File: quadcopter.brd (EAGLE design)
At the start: 228.6 x 228.6 mm, 62 parts, among them J1 AVR_SPI_PRG_6NS, U1 ATMEGA128RFA1, Y1 16MHz

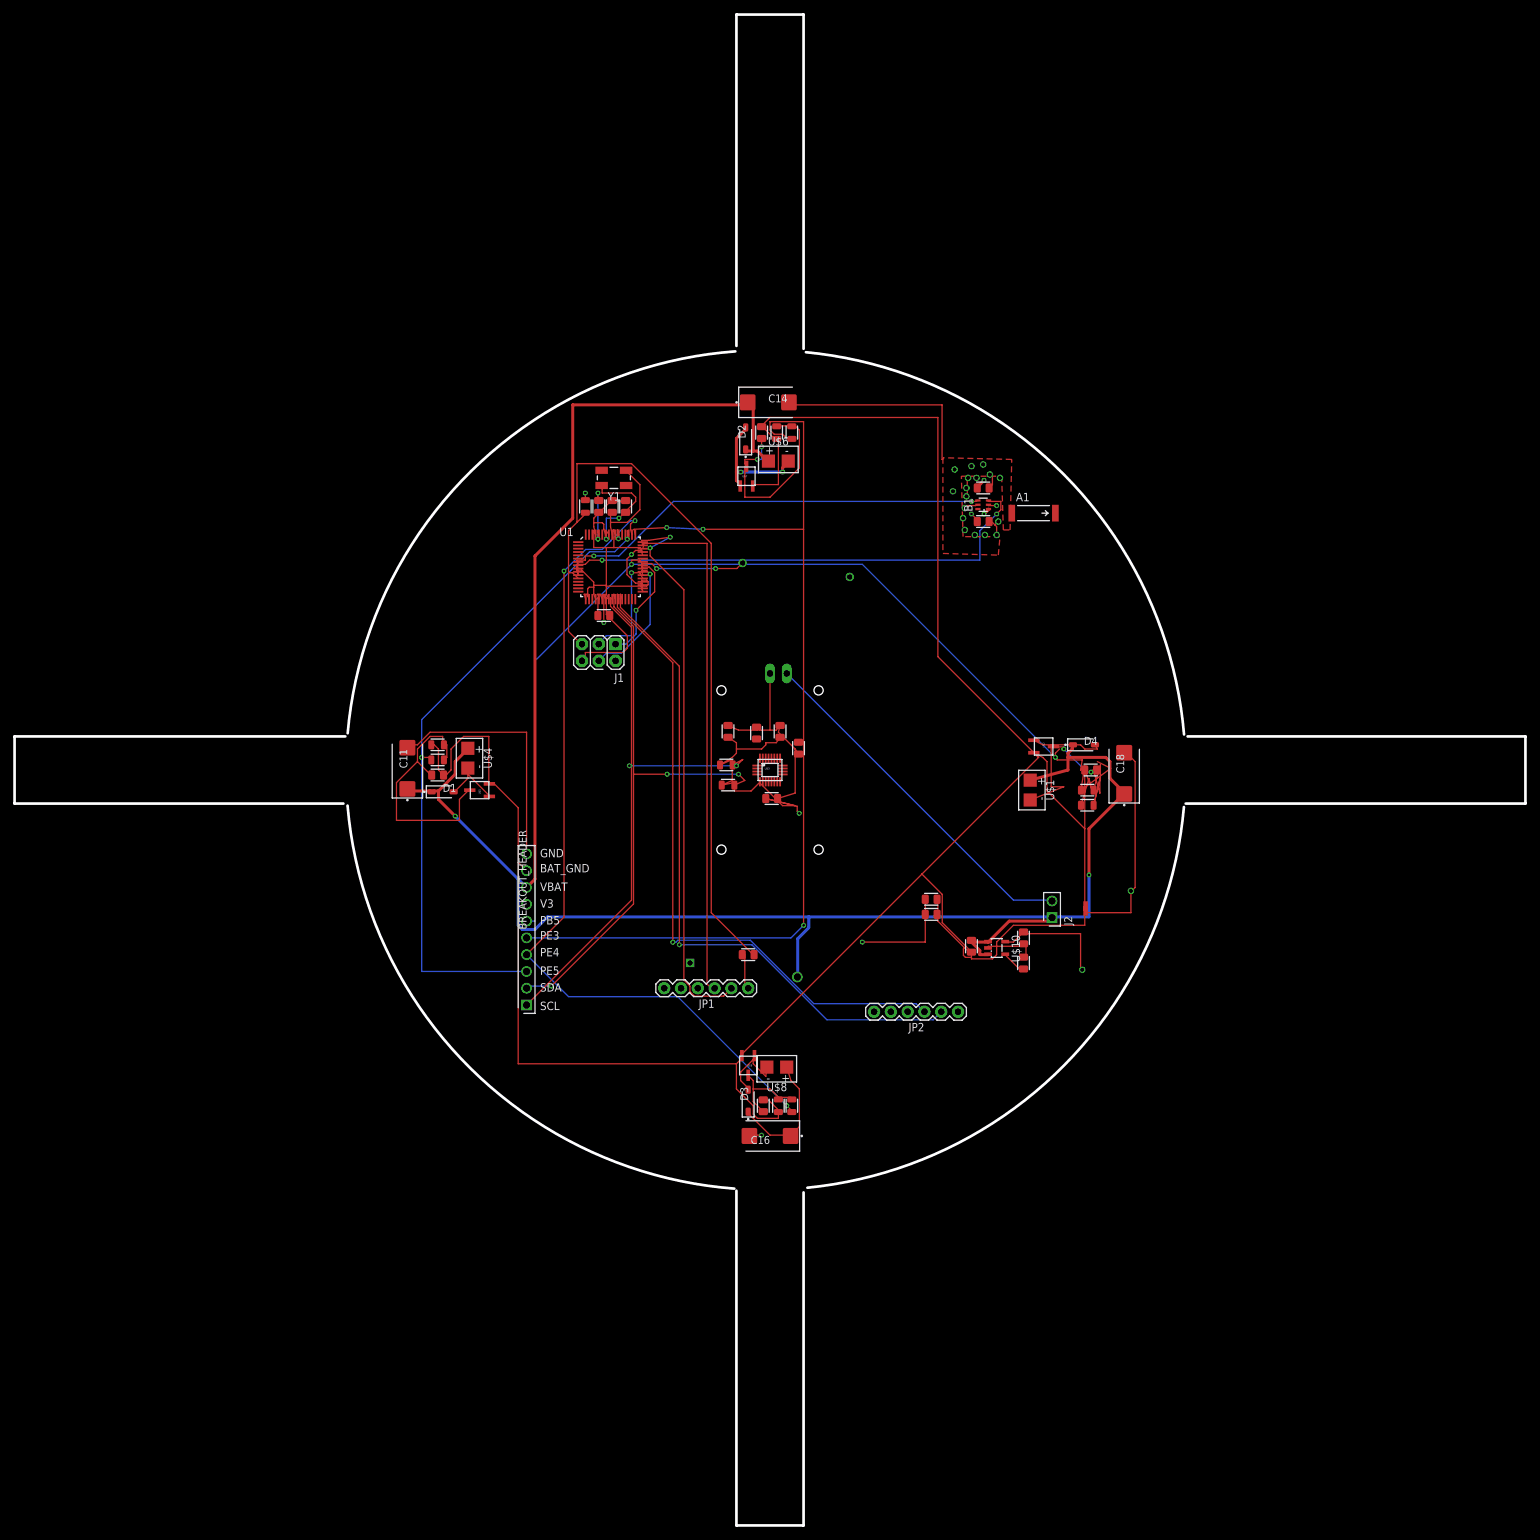
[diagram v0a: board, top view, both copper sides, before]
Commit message: Renamed schematics
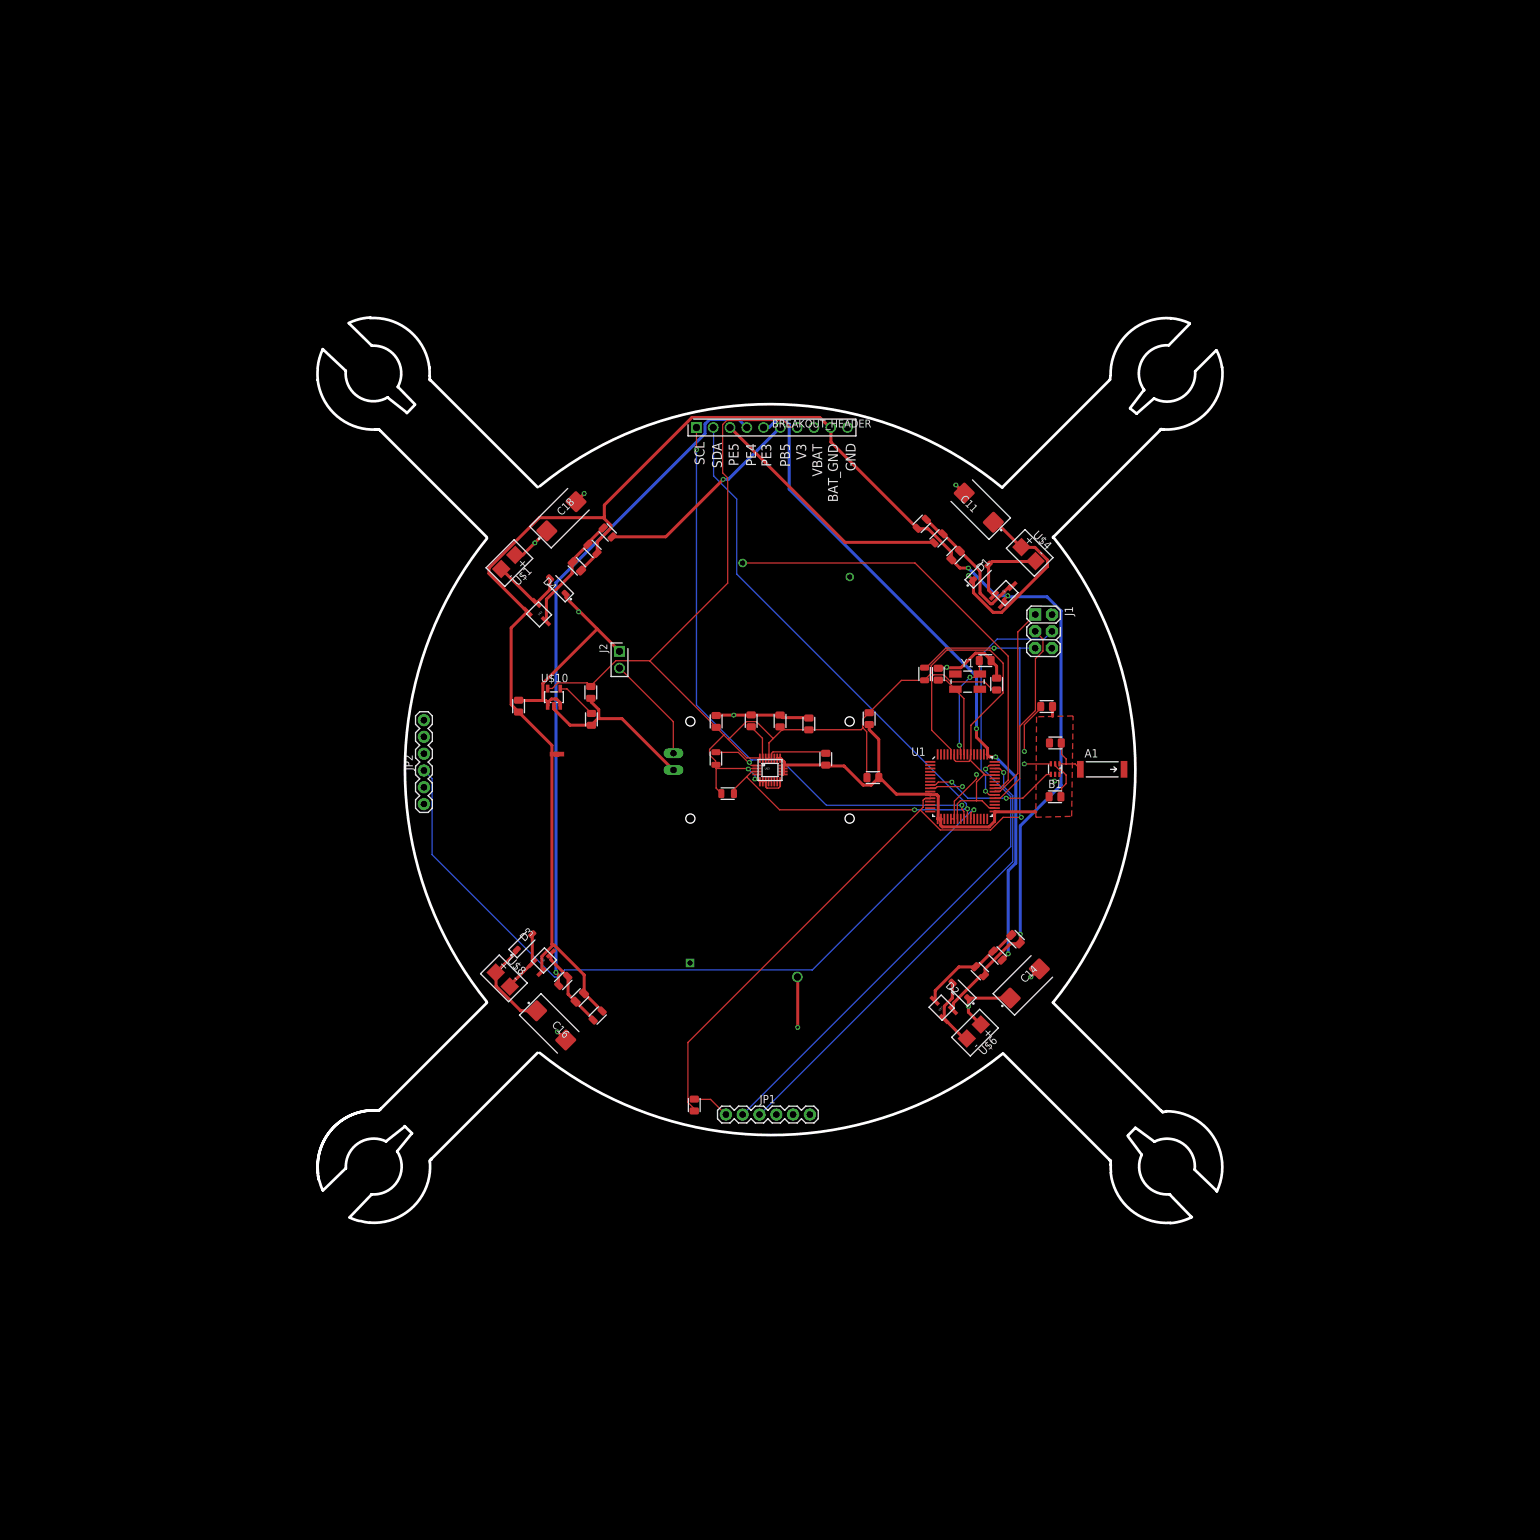
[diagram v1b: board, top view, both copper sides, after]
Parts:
- moved C14 96.1 mm to (38.5, -32.3), turned to 45 degrees
- moved C11 95.0 mm to (31.6, 39.7), turned to 135 degrees
- moved C18 93.6 mm to (-31.6, 38.4), turned to 45 degrees
- moved U$6 91.2 mm to (31.2, -39.2), turned to 225 degrees
- moved BREAKOUT_HEADER 91.1 mm to (-11.1, 51.8), turned to 0 degrees
- moved U$4 89.9 mm to (38.8, 33.0), turned to 315 degrees
- moved D2 89.6 mm to (28.8, -33.4), turned to 135 degrees
- moved D1 87.9 mm to (31.9, 29.9), turned to 45 degrees
- moved R8 87.1 mm to (31.8, -30.4), turned to 135 degrees
- moved JP2 86.7 mm to (-52.4, -5.15), turned to 90 degrees
- moved U$1 85.8 mm to (-39.2, 31.8), turned to 225 degrees
- moved C13 85.7 mm to (37.1, -25.6), turned to 315 degrees
- moved U$7 85.7 mm to (26.0, -36.0), turned to 45 degrees
- moved C7 85.1 mm to (28.1, 32.5), turned to 225 degrees
- moved R7 85.0 mm to (34.4, -28.1), turned to 135 degrees
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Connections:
- net GND: now also JP2.GND
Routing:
- net VBAT: track 313.5 -> 89.5 mm, vias 2 -> 5
- net GND: track 269.3 -> 121.5 mm, vias 19 -> 7
- net PB5: track 160.1 -> 32.3 mm, vias 2 -> 1
- net V3: track 97.3 -> 220.8 mm, vias 7 -> 2
- net TX1: track 102.3 -> 0.00 mm, vias 1 -> 0
- net BAT_GND: track 346.8 -> 272.5 mm, vias 0 -> 3
- net PE5: track 100.0 -> 38.1 mm, vias 2 -> 0
- net N$37: track 74.1 -> 19.8 mm
- net PE3: track 155.6 -> 101.3 mm
- net PB4: track 16.7 -> 67.3 mm, vias 2 -> 0
- net N$36: track 65.5 -> 20.9 mm
- net N$25: track 54.4 -> 16.3 mm
- net SDA: track 89.3 -> 115.9 mm, vias 3 -> 2
- net PE4: track 126.9 -> 101.6 mm, vias 3 -> 1
- net N$41: track 4.85 -> 25.1 mm, vias 0 -> 2
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- added copper zone on layer 15, net GND
- added copper zone on layer 15, net N$30
- added copper zone on layer 2, net N$30
- added copper zone on layer 2, net V3
- added copper zone on layer 2, net VBAT
- removed copper zone on layer 15, net N$3
- removed copper zone on layer 2, net N$3
- removed copper zone on layer 15, net V3
- removed copper zone on layer 15, net VBAT
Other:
- board size 228.6 x 228.6 mm -> 136.9 x 137 mm

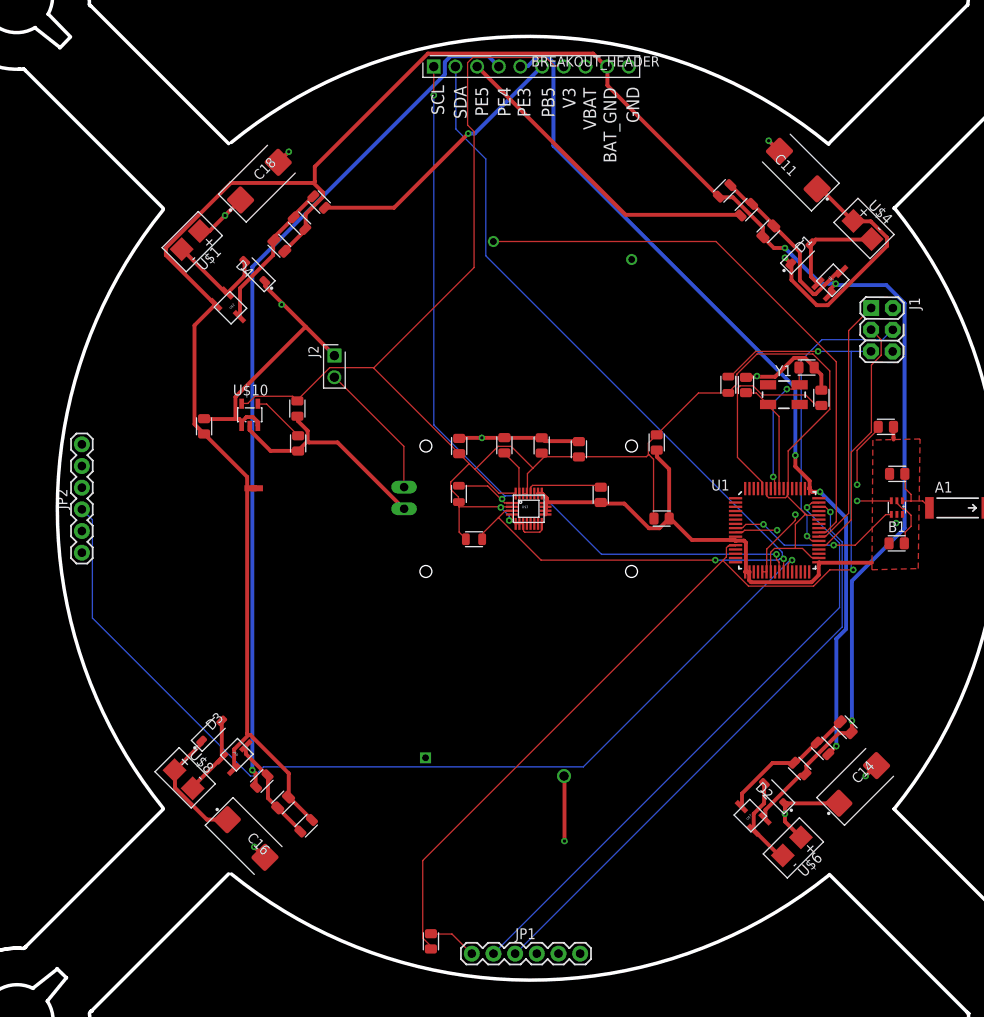
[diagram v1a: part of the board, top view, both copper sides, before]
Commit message: Moved parts around on board, trying to connect air wires
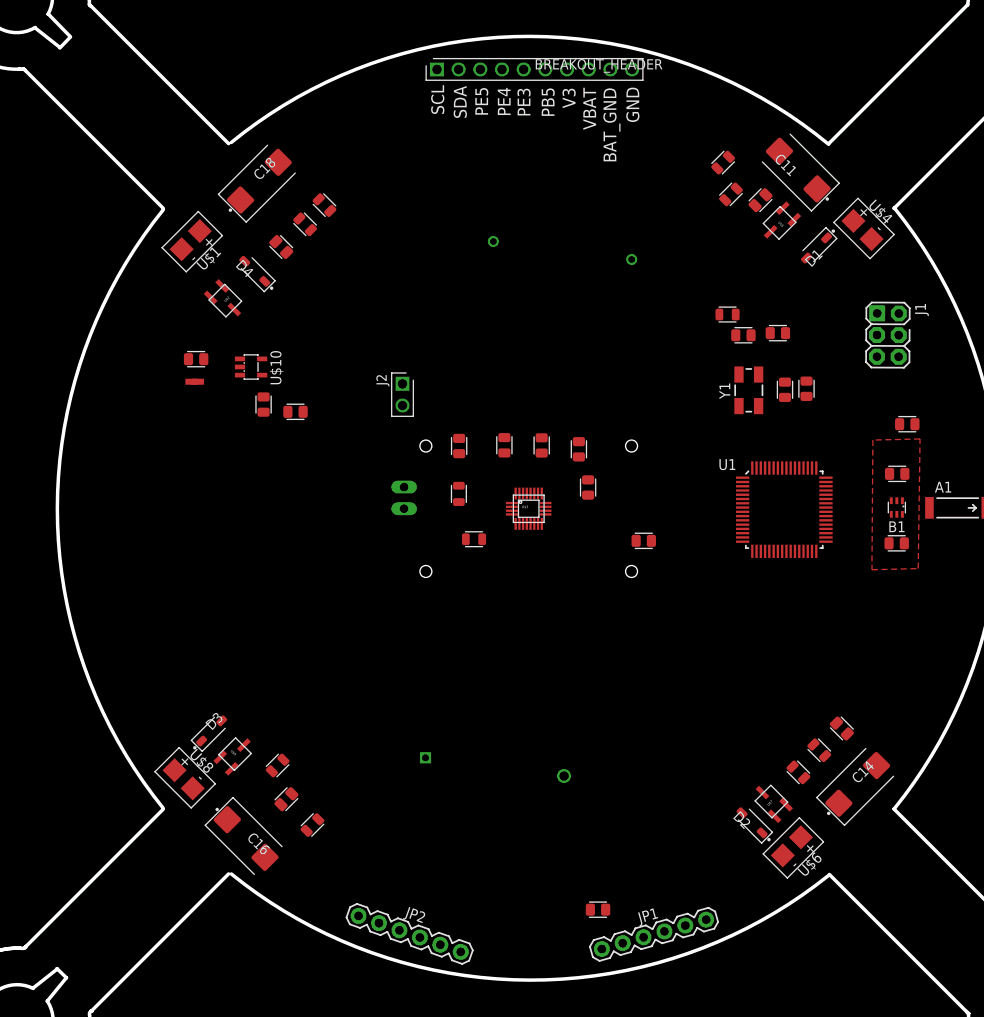
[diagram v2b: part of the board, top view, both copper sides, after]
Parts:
- moved JP2 53.5 mm to (-19.9, -47.7), turned to 340.6 degrees
- moved C10 19.9 mm to (8.12, -47.0), turned to 0 degrees
- moved C6 16.2 mm to (25.2, 20.3), turned to 180 degrees
- moved JP1 15.2 mm to (8.57, -51.6), turned to 15.7 degrees
- moved U$11 14.3 mm to (-39.3, 14.9)
- moved U$5 9.16 mm to (29.4, 33.5), turned to 135 degrees
- moved J2 8.64 mm to (-14.8, 14.6)
- moved R1 8.23 mm to (23.3, 22.8), turned to 0 degrees
- moved C25 7.92 mm to (-39.0, 17.5), turned to 180 degrees
- moved C23 6.09 mm to (-31.1, 12.2)
- moved U$10 5.60 mm to (-32.5, 16.6), turned to 270 degrees
- moved C27 5.25 mm to (29.2, 20.6)
- moved C26 4.60 mm to (30.0, 13.9)
- moved D2 4.32 mm to (26.2, -36.8)
- moved Y1 4.14 mm to (25.8, 13.9), turned to 90 degrees
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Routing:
- net BAT_GND: track 272.5 -> 0.00 mm, vias 3 -> 0
- net V3: track 220.8 -> 0.00 mm, vias 2 -> 0
- net RESET: track 124.4 -> 0.00 mm, vias 2 -> 0
- net GND: track 121.5 -> 0.00 mm, vias 7 -> 0
- net SDA: track 115.9 -> 0.00 mm, vias 2 -> 0
- net RX1: track 115.0 -> 0.00 mm, vias 1 -> 0
- net PE4: track 101.6 -> 0.00 mm, vias 1 -> 0
- net PE3: track 101.3 -> 0.00 mm, vias 3 -> 0
- net SCL: track 98.3 -> 0.00 mm, vias 3 -> 0
- net VBAT: track 89.5 -> 0.00 mm, vias 5 -> 0
- net TX0: track 72.3 -> 0.00 mm, vias 1 -> 0
- net RX0: track 69.8 -> 0.00 mm, vias 1 -> 0
- net PB4: track 67.3 -> 0.00 mm
- net PE5: track 38.1 -> 0.00 mm
- net MOSI: track 34.7 -> 0.00 mm, vias 1 -> 0
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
